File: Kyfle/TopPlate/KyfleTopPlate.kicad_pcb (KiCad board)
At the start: 2 copper layers, 160.8 x 132.8 mm, 33 parts, among them SW2 KEY_SWITCH

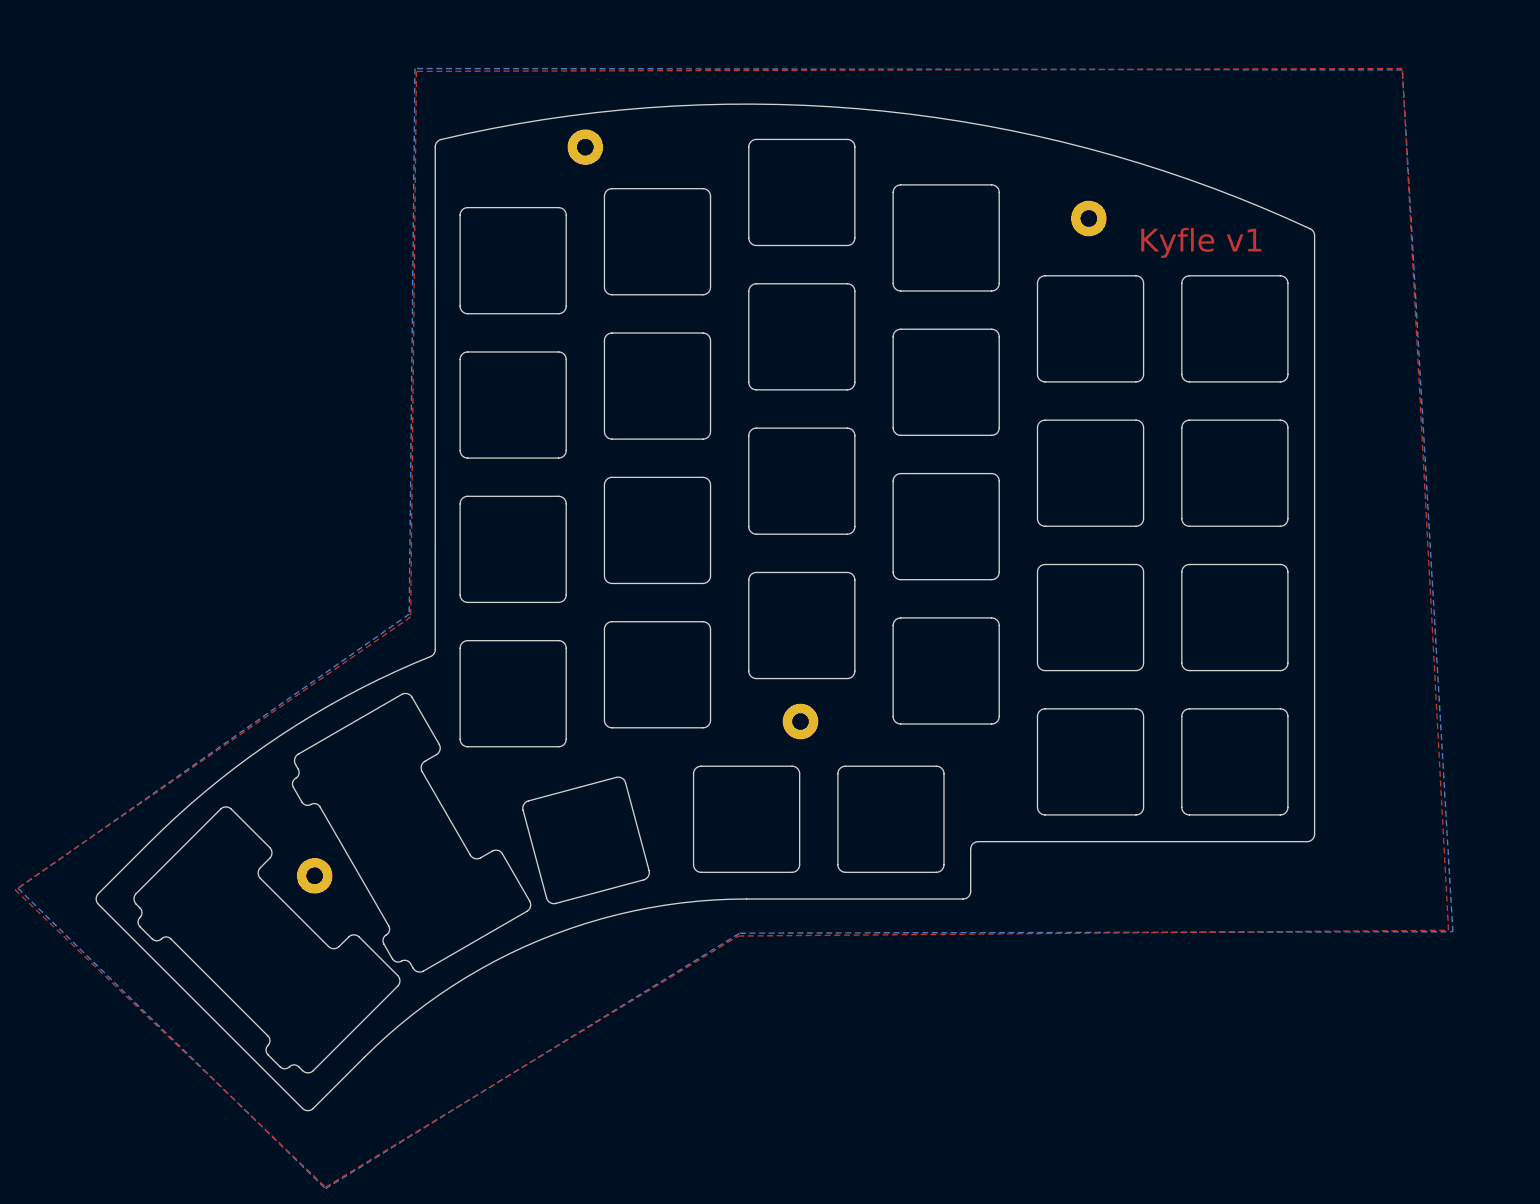
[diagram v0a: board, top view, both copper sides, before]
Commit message: Added tenting holes and reviewed mechanical fixture solutions.
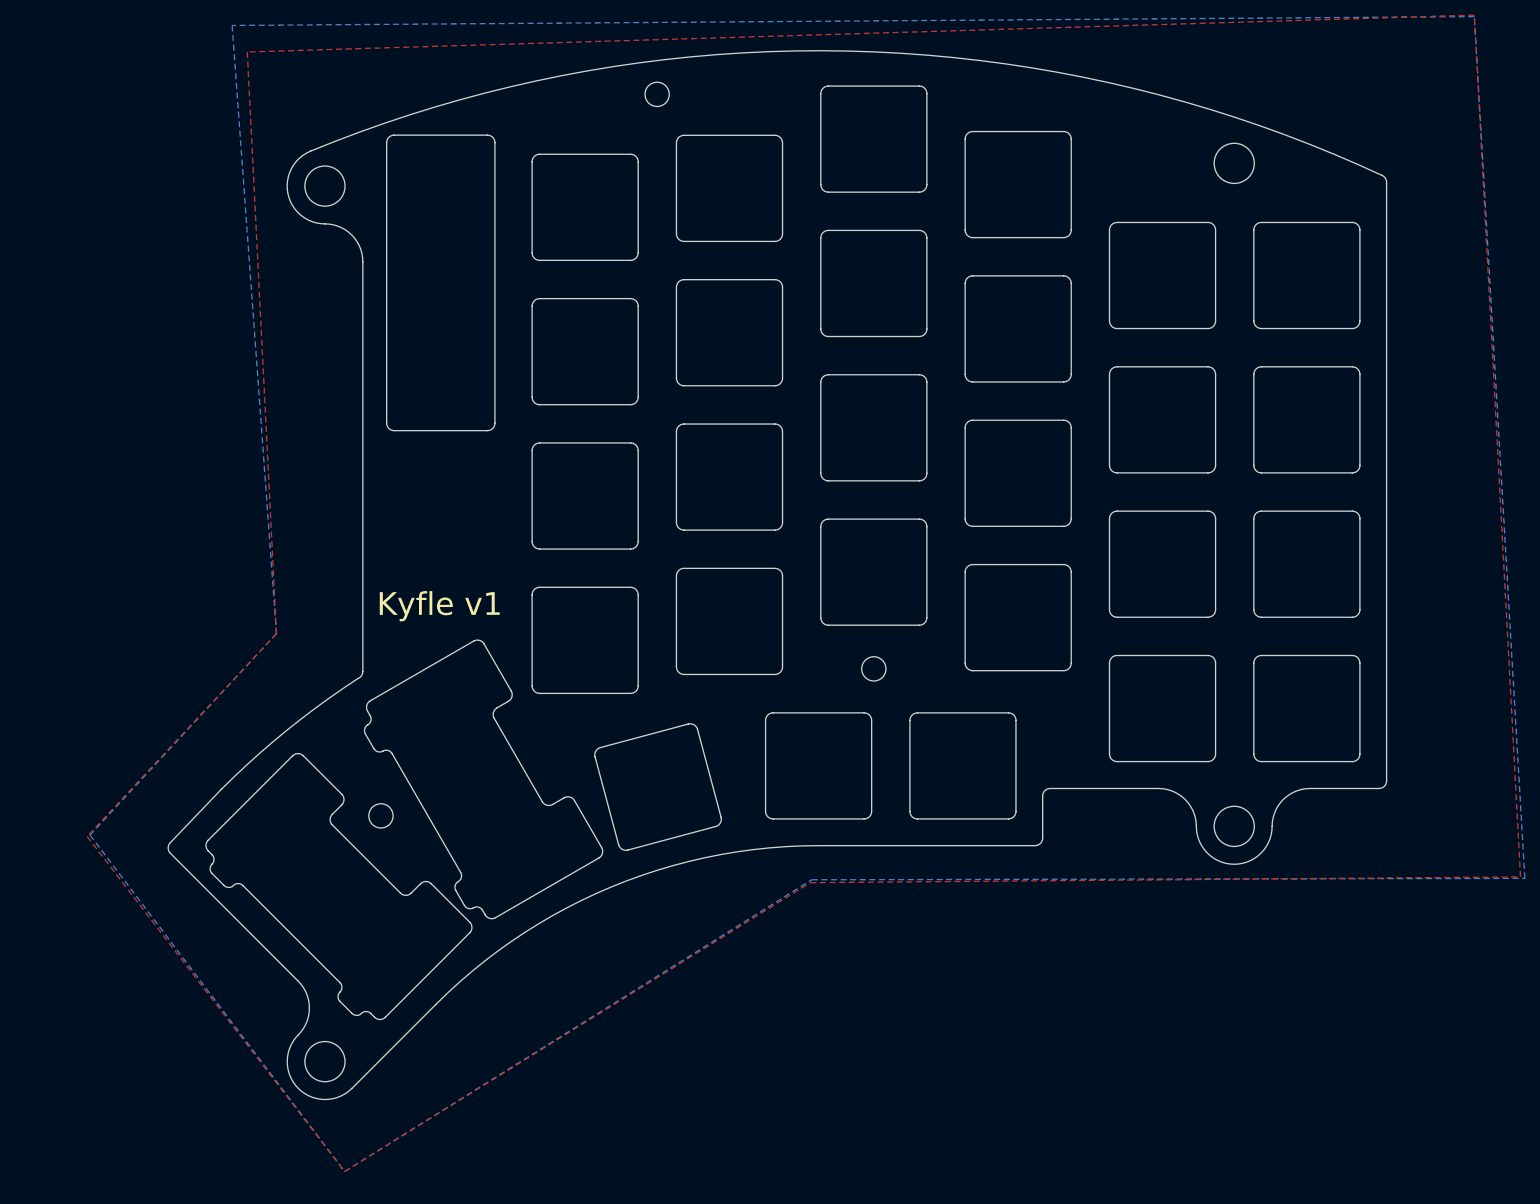
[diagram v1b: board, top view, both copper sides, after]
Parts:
- removed the SW2 at (140.5, 87.0)
- removed the SW2 at (140.5, 106.1)
- removed the SW2 at (140.5, 68.0)
- removed the SW2 at (140.5, 48.9)
- removed the SW2 at (152.3, 125.2)
- removed the SW2 at (159.5, 99.6)
- removed the SW2 at (159.5, 80.5)
- removed the SW2 at (159.5, 61.5)
- removed the SW2 at (159.5, 42.4)
- removed the SW2 at (171.3, 125.2)
- removed the SW2 at (178.6, 105.6)
- removed the SW2 at (87.6, 142.4)
- removed the SW2 at (178.6, 86.5)
- removed the SW2 at (178.6, 67.5)
- removed the SW2 at (178.6, 48.4)
- removed the SW2 at (197.6, 117.6)
- removed the SW2 at (216.7, 98.5)
- removed the SW2 at (197.6, 98.5)
- removed the SW2 at (216.7, 79.5)
- removed the SW2 at (197.6, 79.5)
- removed the SW2 at (197.6, 60.4)
- removed the SW2 at (216.7, 60.4)
- removed the SW2 at (106.6, 127.9)
- removed the SW2 at (131.1, 128.0)
- removed the SW2 at (216.7, 117.6)
- removed the SW2 at (121.4, 108.6)
- removed the SW2 at (121.4, 89.5)
- removed the SW2 at (121.4, 70.5)
- removed the SW2 at (121.4, 51.4)
- removed TH4, TH6: HOLE, SofleKeyboard-footprint:HOLE_M2_TH
- removed the TH7 at (95.3, 132.6)
- added REF**: MountingHole_5.3mm_M5_ISO14580, MountingHole:MountingHole_5.3mm_M5_ISO14580, F.Cu at (96.6, 157.1)
- added REF**: MountingHole_5.3mm_M5_ISO14580, MountingHole:MountingHole_5.3mm_M5_ISO14580, F.Cu at (96.6, 41.6)
- added REF**: MountingHole_5.3mm_M5_ISO14580, MountingHole:MountingHole_5.3mm_M5_ISO14580, F.Cu at (216.6, 126.1)
- added REF**: MountingHole_5.3mm_M5_ISO14580, MountingHole:MountingHole_5.3mm_M5_ISO14580, F.Cu at (216.6, 38.6)
- added SW2: PRO MICRO, SofleChocTop:SU120_ProMicro, F.Cu at (111.9, 63.5)
- added SW2: KEY_SWITCH, SofleChocTop:SW_Hole, F.Cu at (130.9, 44.4)
- added SW2: KEY_SWITCH, SofleChocTop:SW_Hole, F.Cu at (150.0, 99.0)
- added SW2: KEY_SWITCH, SofleChocTop:SW_Hole, F.Cu at (150.0, 61.0)
- added SW2: KEY_SWITCH, SofleChocTop:SW_Hole, F.Cu at (150.0, 41.9)
- added SW2: KEY_SWITCH, SofleChocTop:SW_Hole, F.Cu at (161.8, 118.1)
- added SW2: KEY_SWITCH, SofleChocTop:SW_Hole, F.Cu at (169.1, 92.5)
- added SW2: KEY_SWITCH, SofleChocTop:SW_Hole, F.Cu at (169.1, 73.5)
- added SW2: KEY_SWITCH, SofleChocTop:SW_Hole, F.Cu at (169.1, 54.5)
- added SW2: KEY_SWITCH, SofleChocTop:SW_Hole, F.Cu at (169.1, 35.4)
- added SW2: KEY_SWITCH, SofleChocTop:SW_Hole, F.Cu at (180.8, 118.1)
- added SW2: KEY_SWITCH, SofleChocTop:SW_Hole, F.Cu at (150.0, 80.0)
- added SW2: KEY_SWITCH, SofleChocTop:SW_Hole, F.Cu at (188.1, 98.5)
- added SW2: KEY_SWITCH, SofleChocTop:SW_Hole, F.Cu at (188.1, 79.5)
- added SW2: KEY_SWITCH, SofleChocTop:SW_Hole, F.Cu at (188.1, 60.5)
- added SW2: KEY_SWITCH, SofleChocTop:SW_Hole, F.Cu at (188.1, 41.4)
- added SW2: KEY_SWITCH, SofleChocTop:SW_Hole, F.Cu at (207.2, 110.5)
- added SW2: KEY_SWITCH, SofleChocTop:SW_Hole, F.Cu at (226.2, 91.5)
- added SW2: KEY_SWITCH, SofleChocTop:SW_Hole, F.Cu at (207.2, 91.5)
- added SW2: KEY_SWITCH, SofleChocTop:SW_Hole, F.Cu at (226.2, 72.5)
- added SW2: KEY_SWITCH, SofleChocTop:SW_Hole, F.Cu at (207.2, 72.5)
- added SW2: KEY_SWITCH, SofleChocTop:SW_Hole, F.Cu at (207.2, 53.4)
- added SW2: KEY_SWITCH, SofleChocTop:SW_Hole_2u, F.Cu at (97.1, 135.4)
- added SW2: KEY_SWITCH, SofleChocTop:SW_Hole, F.Cu at (226.2, 53.4)
- added SW2: KEY_SWITCH, SofleChocTop:SW_Hole_2u, F.Cu at (116.1, 120.8)
- added SW2: KEY_SWITCH, SofleChocTop:SW_Hole, F.Cu at (140.6, 120.9)
- added SW2: KEY_SWITCH, SofleChocTop:SW_Hole, F.Cu at (226.2, 110.5)
- added SW2: KEY_SWITCH, SofleChocTop:SW_Hole, F.Cu at (130.9, 101.5)
- added SW2: KEY_SWITCH, SofleChocTop:SW_Hole, F.Cu at (130.9, 82.5)
- added SW2: KEY_SWITCH, SofleChocTop:SW_Hole, F.Cu at (130.9, 63.5)
- added TH7: HOLE, MountingHole:MountingHole_3.2mm_M3_ISO14580, F.Cu at (169.1, 105.3)
- added TH7: HOLE, MountingHole:MountingHole_3.2mm_M3_ISO14580, F.Cu at (104.0, 124.7)
- TH3: footprint SofleKeyboard-footprint:HOLE_M2_TH -> MountingHole:MountingHole_3.2mm_M3_ISO14580
- moved TH3 11.8 mm to (140.4, 29.5)
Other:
- board size 160.8 x 132.8 mm -> 160.8 x 138.4 mm

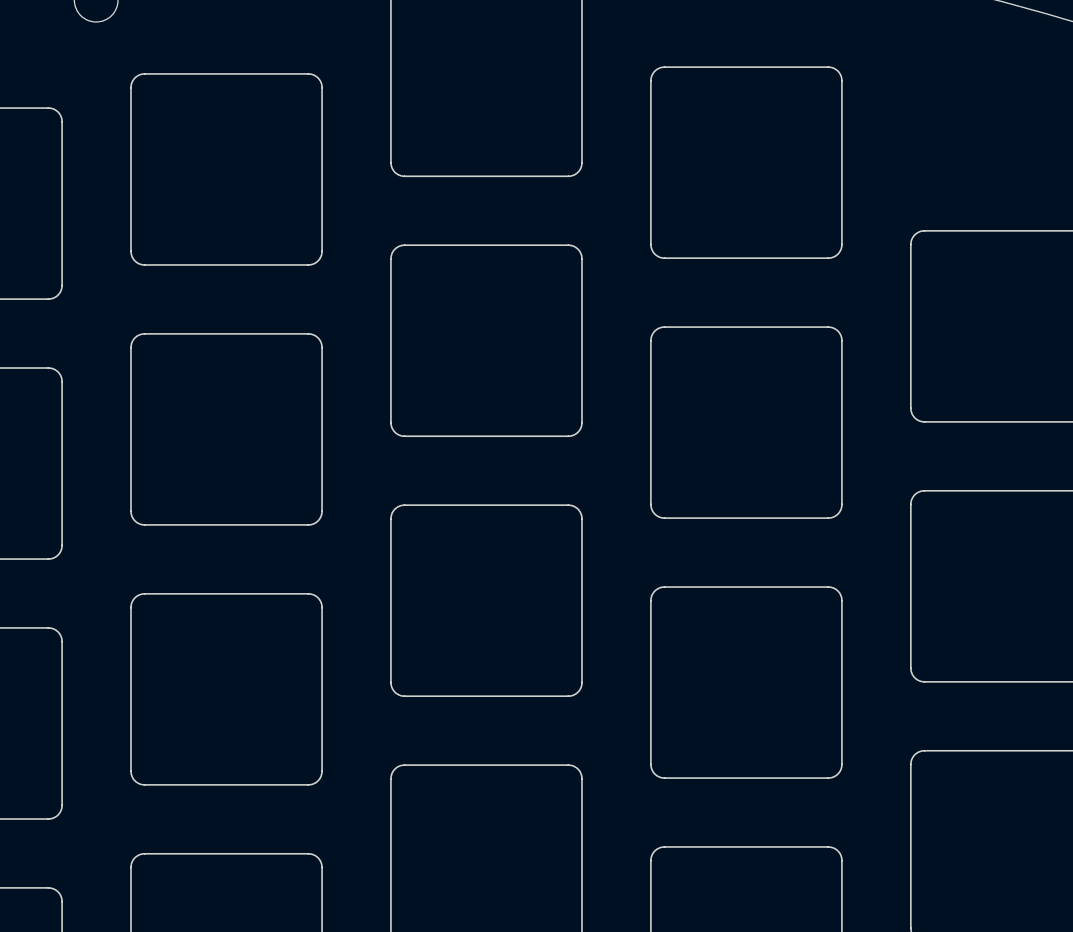
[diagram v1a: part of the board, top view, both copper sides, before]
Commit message: Working on solutions to hold the main PCB.
Also cleaned a bit the layers by separating physical dimensions (CrtYrd), functional wiring (Fab) and other construction lines (User).
Completed the wiring template.
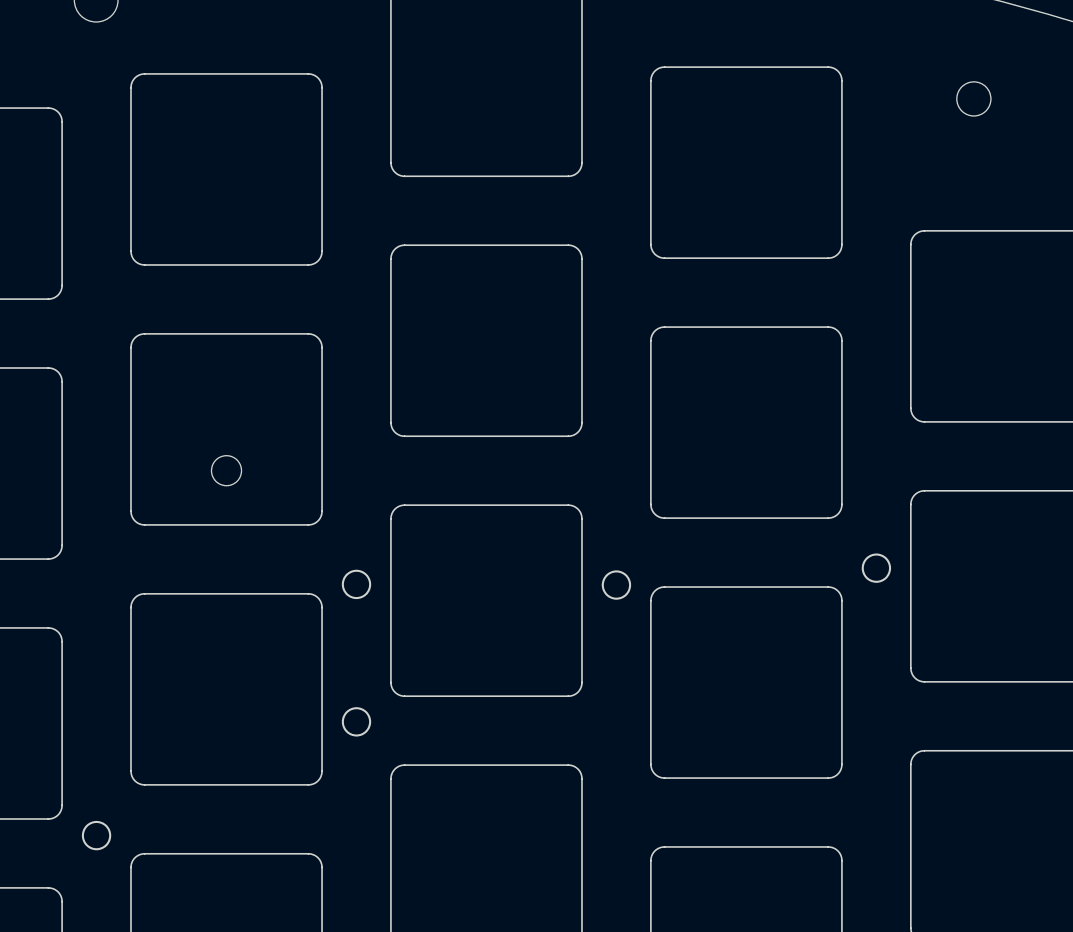
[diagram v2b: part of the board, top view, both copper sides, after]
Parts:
- added REF**: MountingHole_2.2mm_M2_ISO14580, MountingHole:MountingHole_2.2mm_M2_ISO14580, F.Cu at (150.0, 64.0)
- added SW2: KEY_SWITCH, SofleChocTop:SK6812_Bit, F.Cu at (204.8, 36.7)
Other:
- outline, holes or cut-outs redrawn
